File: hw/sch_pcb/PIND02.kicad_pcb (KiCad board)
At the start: 2 copper layers, 40.1 x 40.1 mm, 56 parts, among them J1 Conn_Coaxial, J2 HEADER_2x05_PARALLEL, J3 HEADER_2x01, M1 HOLE M3, M2 HOLE M3, M3 HOLE, M4 HOLE, Q1 2SK2394-6, U1 OPA2314, U2 ISL21080DIH312Z-TK, U3 SHT31-DIS, U4 TPS613222ADBV

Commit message: PCB design WIP.
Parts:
- added M5: RFShield_TwoPieces, RF_Shielding:Laird_Technologies_BMI-S-204-F_32.00x32.00mm, B.Cu at (148.5, 105.0)
- C10, C23, C24, C4, C7, C9: footprint Capacitor_SMD:C_0603_1608Metric -> Capacitor_Tantalum_SMD:CP_EIA-3216-18_Kemet-A; moved to B.Cu
- C11, C13, C14, C20, C3, C6: footprint Capacitor_SMD:C_0603_1608Metric -> Capacitor_SMD:C_0805_2012Metric; moved to B.Cu
- C12, C15, C5: footprint Capacitor_SMD:C_0603_1608Metric -> Capacitor_SMD:C_1210_3225Metric; moved to B.Cu
- C16, C17, C18, C19, C21, C22, C8, FID1, FID2, JP1, L1, L2, L3, Q1, R1, R11, R2, R3, R5, R6, R7, R8, R9, U1, U2, U3, U4: moved to B.Cu
- J2: value HEADER_2x05_PARALLEL -> MLAB I2C interface
- R10, R4: footprint Resistor_SMD:R_0603_1608Metric -> Resistor_SMD:R_0805_2012Metric; moved to B.Cu
- R12: footprint Mlab_R:SMD-0805 -> Resistor_SMD:R_0805_2012Metric; moved to B.Cu
- moved L1 104.0 mm to (104.6, 108.7), turned to 180 degrees
- moved C24 101.5 mm to (93.8, 75.0), turned to 180 degrees
- moved U3 99.1 mm to (111.4, 108.0), turned to 180 degrees
- moved L2 97.9 mm to (110.4, 90.0), turned to 180 degrees
- moved C20 93.8 mm to (97.8, 80.0), turned to 180 degrees
- moved C21 93.8 mm to (97.8, 82.6), turned to 180 degrees
- moved C22 93.8 mm to (97.8, 85.1), turned to 180 degrees
- moved C23 93.8 mm to (97.8, 87.6), turned to 180 degrees
- moved C17 88.3 mm to (111.9, 112.6), turned to 180 degrees
- moved FID2 82.5 mm to (129.1, 122.9), turned to 180 degrees
- moved U4 79.6 mm to (105.2, 91.1), turned to 180 degrees
- moved J2 79.0 mm to (122.0, 109.1)
- moved JP1 78.4 mm to (114.0, 103.5), turned to 180 degrees
- moved U2 69.9 mm to (136.8, 117.6), turned to 180 degrees
- moved C19 61.0 mm to (128.4, 95.9), turned to 180 degrees
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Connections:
- C10 pad 2: GND -> GNDA
- C11 pad 2: GND -> GNDA
- C15 pad 2: GND -> GNDA
- C18 pad 2: GND -> GNDA
- C20 pad 2: GND -> GNDA
- C3 pad 2: GND -> GNDA
- C4 pad 2: GND -> GNDA
- C6 pad 2: GND -> GNDA
- C7 pad 2: GND -> GNDA
- C9 pad 2: GND -> GNDA
- R3 pad 2: GND -> GNDA
- U1 pad 4: GND -> GNDA
- U2 pad 3: GND -> GNDA
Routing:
- added copper zone on B.Cu, net GNDA
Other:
- board size 40.1 x 40.1 mm -> 60.5 x 40.1 mm

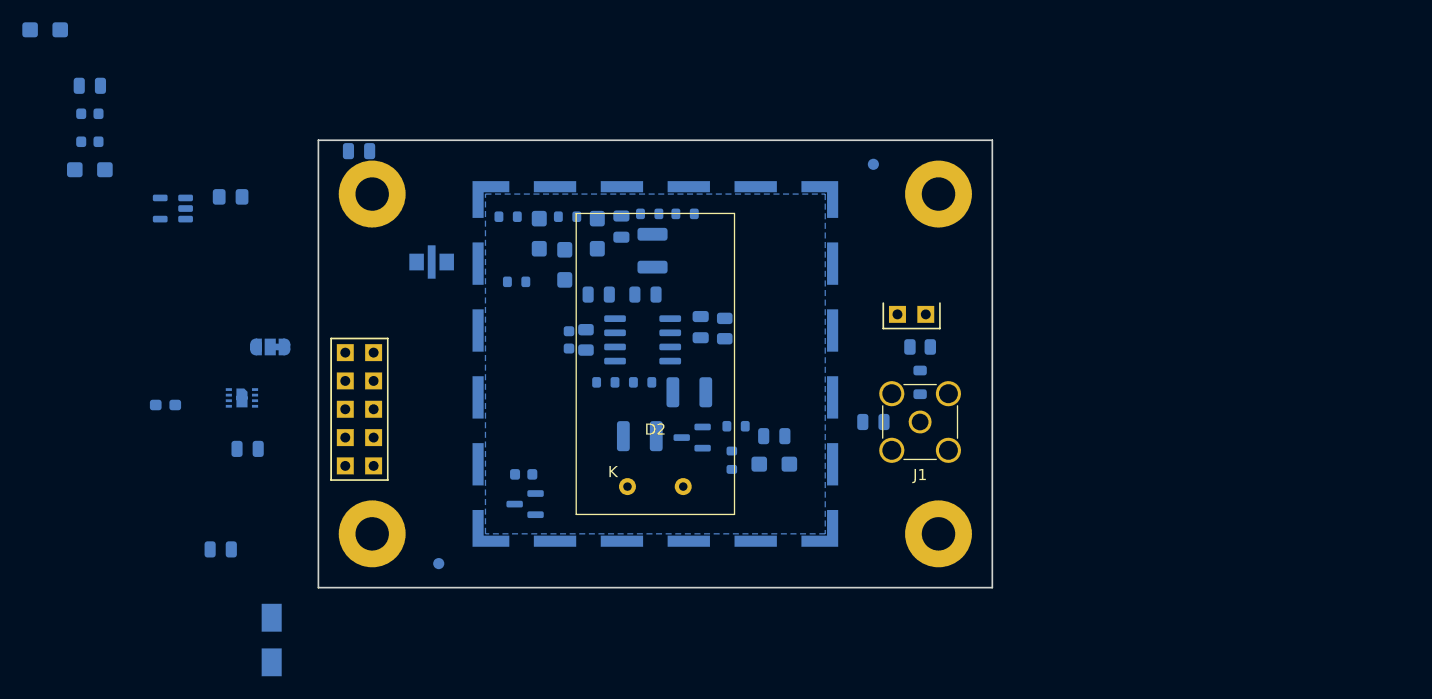
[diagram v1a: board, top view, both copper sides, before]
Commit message: The first fully routed PCB.
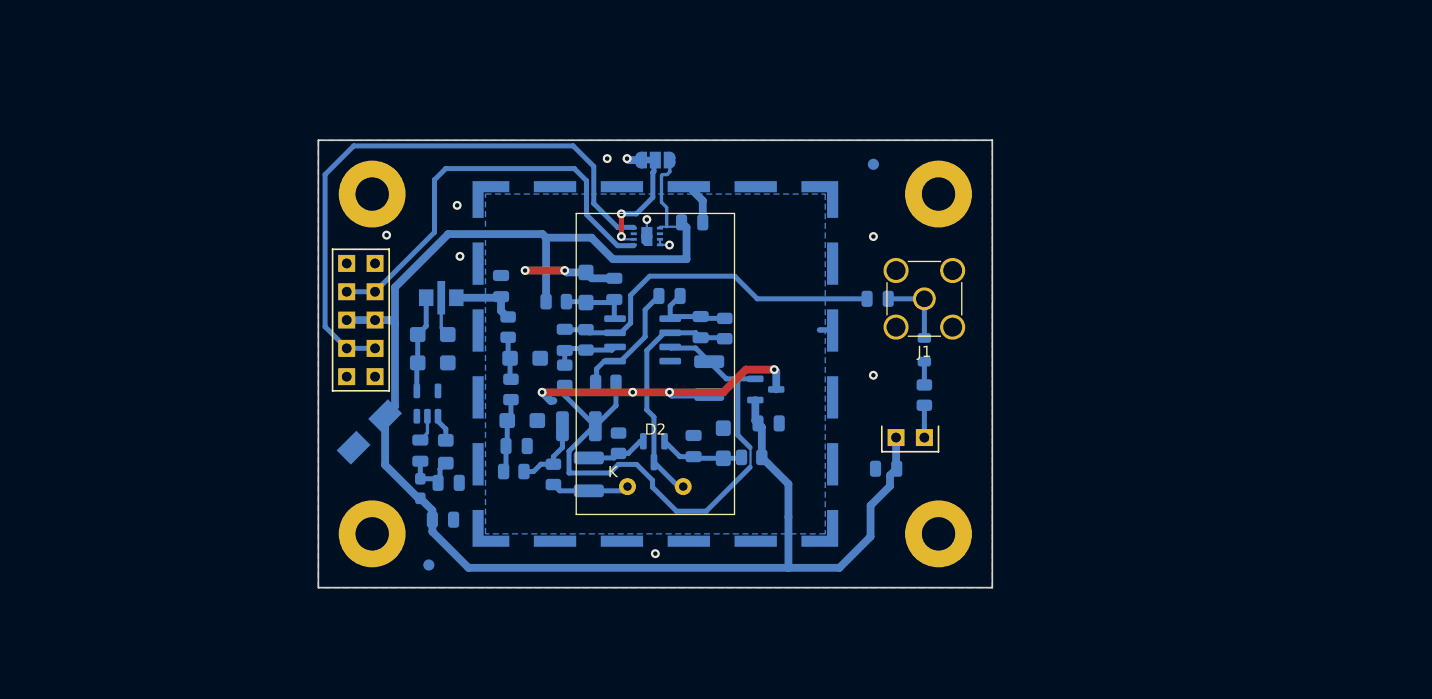
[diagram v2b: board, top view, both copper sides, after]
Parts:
- added JP2: Jumper_2_Bridged, NetTie:NetTie-2_SMD_Pad0.5mm, B.Cu at (163.7, 102.0)
- C16, C18, C21, C22: footprint Capacitor_SMD:C_0603_1608Metric -> Capacitor_SMD:C_0805_2012Metric
- R1, R11, R2, R3, R5, R6, R7, R8, R9: footprint Resistor_SMD:R_0603_1608Metric -> Resistor_SMD:R_0805_2012Metric
- moved C1 60.1 mm to (169.2, 114.4)
- moved C21 46.2 mm to (130.0, 115.7), turned to 0 degrees
- moved C24 45.8 mm to (128.5, 104.9), turned to 0 degrees
- moved C17 44.8 mm to (151.8, 92.3), turned to 0 degrees
- moved C20 41.0 mm to (134.7, 98.0), turned to 90 degrees
- moved C22 40.6 mm to (127.4, 112.8), turned to 90 degrees
- moved U3 39.1 mm to (147.7, 93.6), turned to 0 degrees
- moved JP1 38.4 mm to (148.5, 86.7), turned to 0 degrees
- moved C23 34.1 mm to (128.5, 102.4), turned to 0 degrees
- moved C2 33.9 mm to (129.4, 119.0), turned to 0 degrees
- moved L2 29.9 mm to (129.7, 112.9), turned to 90 degrees
- moved U4 28.8 mm to (128.1, 108.6), turned to 90 degrees
- moved R8 26.2 mm to (139.4, 114.9), turned to 90 degrees
- moved R7 26.1 mm to (135.8, 114.7)
- moved L1 24.1 mm to (127.4, 116.2), turned to 90 degrees
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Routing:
- net VDD: track 0.00 -> 144.2 mm
- net Net-(U3-SCL): track 0.00 -> 52.7 mm
- net /REF: track 0.00 -> 52.4 mm
- net Net-(U3-SDA): track 0.00 -> 37.7 mm
- net GNDA: track 0.00 -> 36.8 mm, vias 0 -> 6
- net Net-(C14-Pad2): track 0.00 -> 31.7 mm
- net /A: track 0.00 -> 21.7 mm
- net GND: track 0.00 -> 13.7 mm, vias 0 -> 10
- net Net-(U1B-+): track 0.00 -> 10.9 mm
- net Net-(JP1-C): track 0.00 -> 10.1 mm, vias 0 -> 2
- net Net-(U4-VOUT): track 0.00 -> 8.71 mm
- net Net-(Q1-D): track 0.00 -> 7.65 mm
- net Net-(C13-Pad2): track 0.00 -> 7.44 mm
- net /K: track 0.00 -> 7.19 mm
- net Net-(C12-Pad1): track 0.00 -> 7.09 mm
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- added copper zone on B.Cu, net GND
- added copper zone on F.Cu, net GND

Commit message: Add silcreen texts.
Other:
- board text added: "GND"
- board text added: "Kaklik 2023"
- board text added: "OUT"
- board text added: "PIND02A"
- board text added: "SCL"
- board text added: "SDA"
- board text added: "Signal+Bias"
- board text added: "VDD"
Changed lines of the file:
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@@
   (gr_rect (start 118.274 84.934) (end 178.726 125.066)
     (stroke (width 0.15) (type default)) (fill none) (layer "Edge.Cuts"))
+  (gr_text "SDA" (at 125.005 99.285) (layer "F.SilkS")
+    (effects (font (size 1 1) (thickness 0.127)) (justify left bottom))
+  )
+  (gr_text "VDD" (at 125.005 101.825) (layer "F.SilkS")
+    (effects (font (size 1 1) (thickness 0.127)) (justify left bottom))
+  )
+  (gr_text "Signal+Bias" (at 166.788 109.445) (layer "F.SilkS")
+    (effects (font (size 1 1) (thickness 0.127)) (justify left bottom))
+  )
+  (gr_text "GND" (at 124.878 106.651) (layer "F.SilkS")
+    (effects (font (size 1 1) (thickness 0.127)) (justify left bottom))
+  )
+  (gr_text "OUT" (at 168.312 100.555 90) (layer "F.SilkS")
+    (effects (font (size 1 1) (thickness 0.127)) (justify left bottom))
+  )
+  (gr_text "Kaklik 2023" (at 127.545 124.05) (layer "F.SilkS")
+    (effects (font (size 1 1) (thickness 0.127)) (justify left bottom))
+  )
+  (gr_text "PIND02A" (at 159.93 124.177) (layer "F.SilkS")
+    (effects (font (size 1.5 1.5) (thickness 0.127)) (justify left bottom))
+  )
+  (gr_text "SCL" (at 125.005 104.238) (layer "F.SilkS")
+    (effects (font (size 1 1) (thickness 0.127)) (justify left bottom))
+  )
+  (gr_text "GND" (at 124.878 96.618) (layer "F.SilkS")
+    (effects (font (size 1 1) (thickness 0.127)) (justify left bottom))
+  )
   (segment (start 134.657 100.238) (end 135.292 100.873) (width 0.7) (layer "B.Cu") (net 1))
   (segment (start 134.657 98.965) (end 134.657 100.238) (width 0.7) (layer "B.Cu") (net 1))
